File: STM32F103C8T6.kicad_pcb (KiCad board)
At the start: 2 copper layers, 39.4 x 77.5 mm, 55 parts, among them J1 USB_Device, J2 USB_TTL, P1 L-Pin, P2 R-Pin, P3 DEBUG, P4 POWER-R, P5 POWER-L, SW1 NRST, U1 MIC5219-3.3YM5, U2 CH340E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

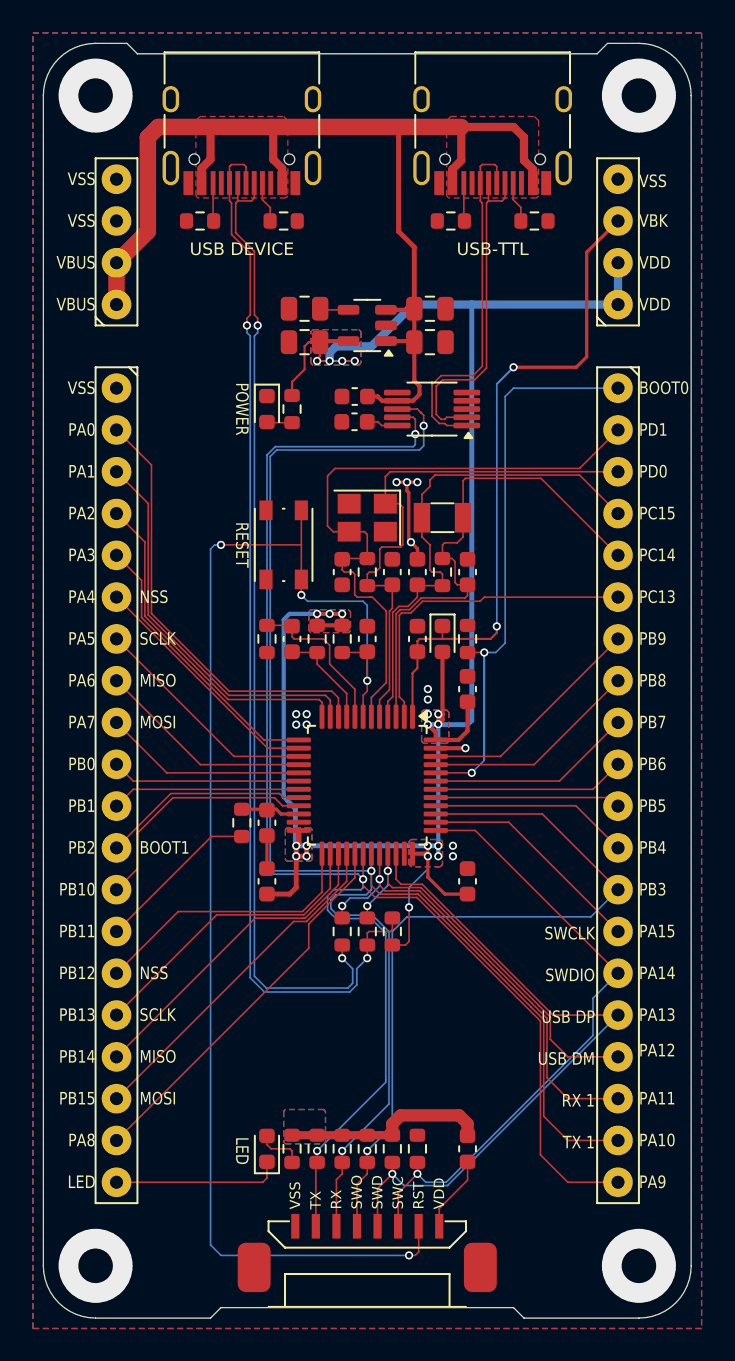
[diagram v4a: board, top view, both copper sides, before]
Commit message: 优化电源走线
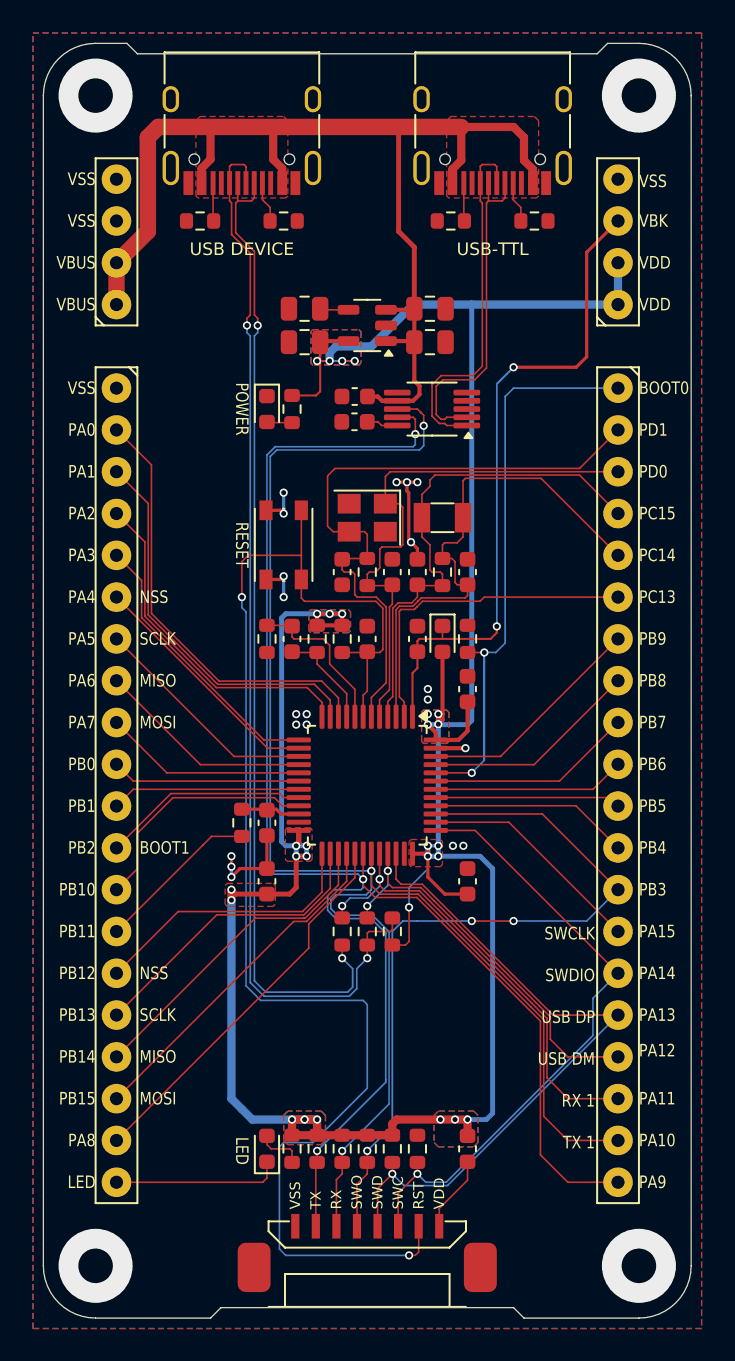
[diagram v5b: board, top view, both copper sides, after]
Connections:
- C15 pad 1: VSS -> VDD
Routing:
- net VDD: track 140.0 -> 191.5 mm, vias 20 -> 28
- net VSS: track 10.0 -> 18.5 mm, vias 13 -> 20
- net /NRST: track 82.1 -> 85.5 mm, vias 4 -> 2
- net /USBF_N: track 59.8 -> 60.4 mm
- net /USBF_P: track 64.9 -> 65.4 mm
- net /PB3/SWO: vias 1 -> 3

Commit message: 更新引脚链接，增加晶振引脚的跳接焊盘
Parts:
- added H1: M2 Hole, Append_Connector:Hole_2×4.5mm, F.Cu at (133.5, 82.5)
- added H2: M2 Hole, Append_Connector:Hole_2×4.5mm, F.Cu at (166.5, 82.5)
- added H3: M2 Hole, Append_Connector:Hole_2×4.5mm, F.Cu at (133.5, 153.7)
- added H4: M2 Hole, Append_Connector:Hole_2×4.5mm, F.Cu at (166.5, 153.7)
- added TP1: PD1, Append_Connector:PAD_Semicircular_1mm, F.Cu at (147.6, 109.1)
- added TP2: PD0, Append_Connector:PAD_Semicircular_1mm, F.Cu at (151.1, 106.2)
- added TP3: PC15, Append_Connector:PAD_Semicircular_1mm, F.Cu at (153.3, 106.8)
- added TP4: PC14, Append_Connector:PAD_Semicircular_1mm, F.Cu at (155.8, 106.8)
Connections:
- P2 pad 2: /PD1/OSC_OUT -> /PD1
- P2 pad 3: /PD0/OSC_IN -> /PD0
- P2 pad 4: /PC15/OSC32_OUT -> /PC15
- P2 pad 5: /PC14/OSC32_IN -> /PC14
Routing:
- net /PD1/OSC_OUT: track 39.5 -> 16.2 mm
- net /PD1: track 0.00 -> 23.1 mm
- net /PD0/OSC_IN: track 33.5 -> 17.6 mm
- net /PC15/OSC32_OUT: track 30.7 -> 15.7 mm
- net /PD0: track 0.00 -> 14.7 mm
- net /PC14/OSC32_IN: track 31.9 -> 18.2 mm
- net /PC15: track 0.00 -> 13.6 mm
- net /PC14: track 0.00 -> 12.0 mm
- net /PB3/SWO: track 46.7 -> 47.2 mm
- net VSS: track 18.5 -> 18.1 mm, vias 20 -> 19
- net (no net): vias 4 -> 0

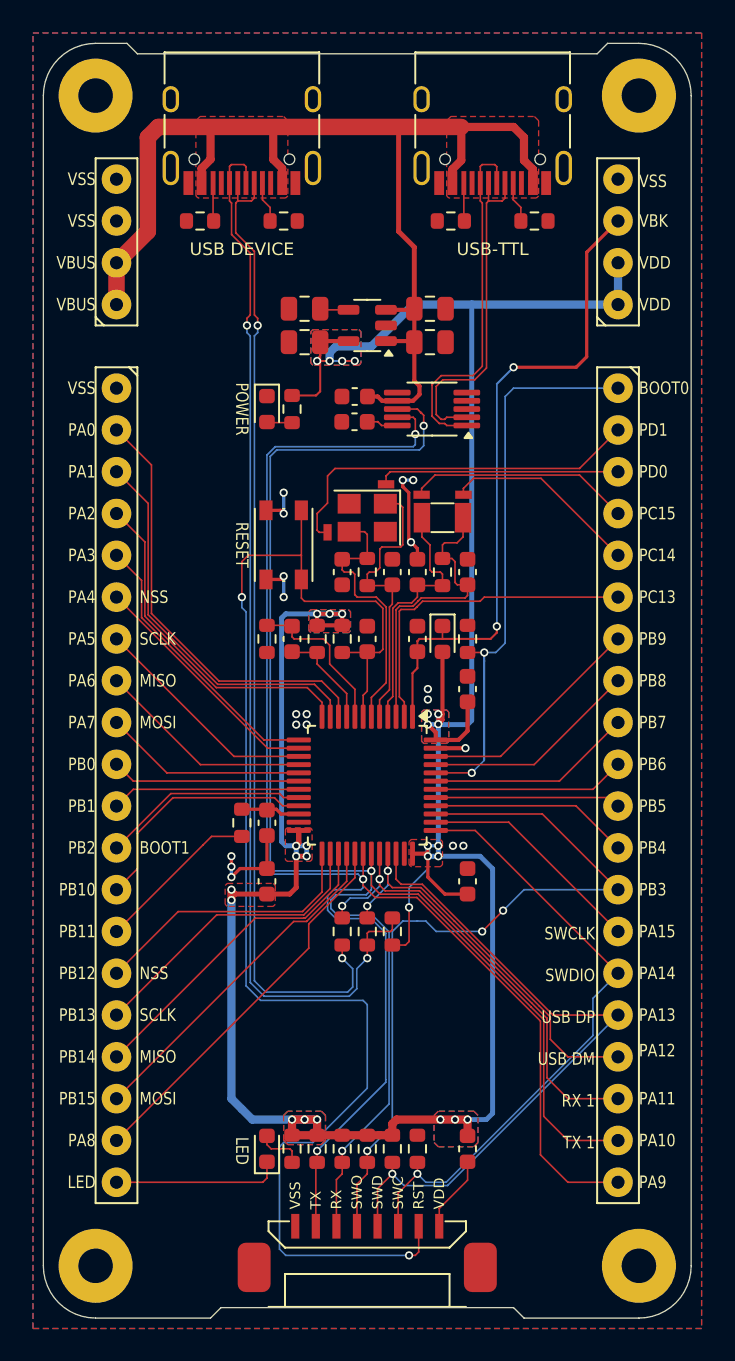
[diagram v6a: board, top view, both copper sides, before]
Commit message: 优化电源走线
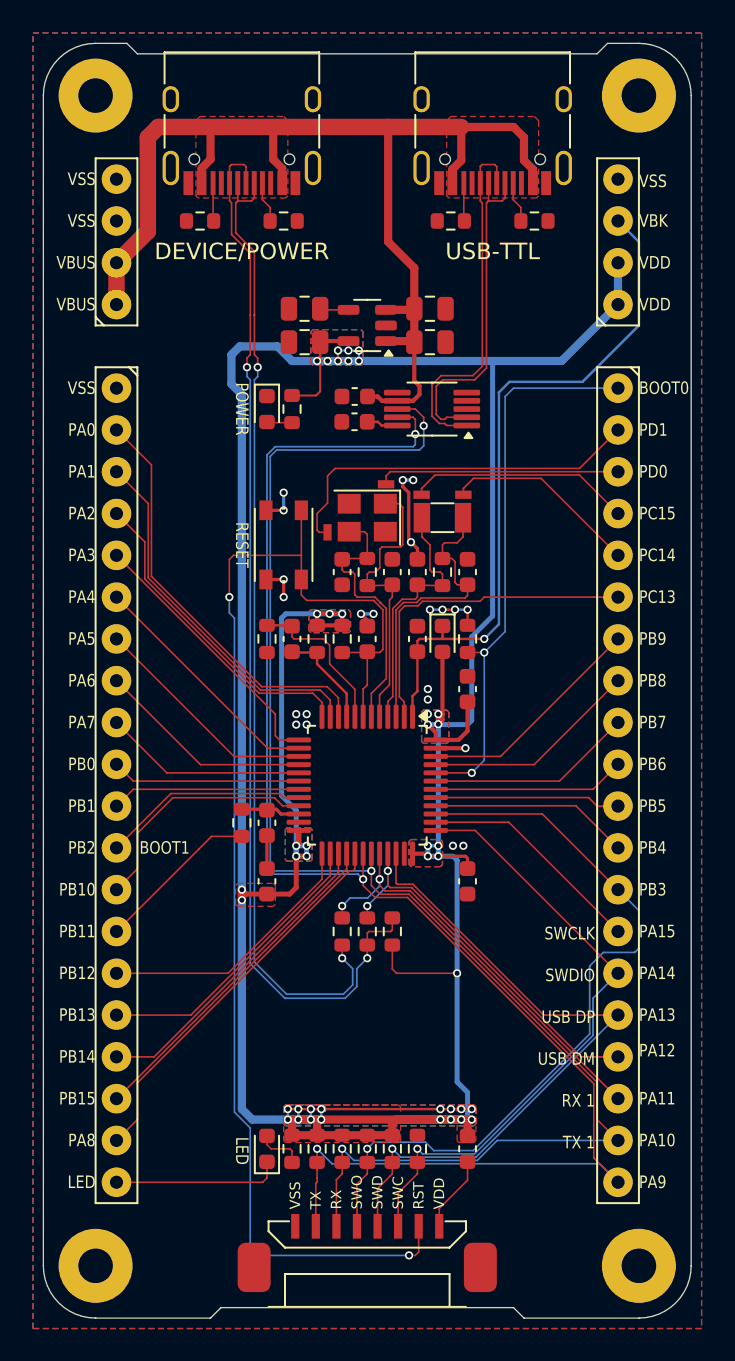
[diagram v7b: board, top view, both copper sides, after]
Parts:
- turned C15 to -90 degrees
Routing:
- net VDD: track 191.5 -> 248.5 mm, vias 28 -> 42
- net VBUS: track 86.6 -> 72.0 mm
- net /PA10/USART_RX: track 99.3 -> 91.5 mm
- net /NRST: track 85.5 -> 78.2 mm
- net /BOOT0: track 41.1 -> 34.0 mm
- net /PA9/USART_TX: track 100.5 -> 94.7 mm
- net /PA11/USBDM: track 27.9 -> 25.7 mm
- net /PA0/WAKEUP: track 26.7 -> 25.3 mm
- net /PA1: track 23.7 -> 22.4 mm
- net /PA2: track 20.8 -> 19.4 mm
- net VBAT: track 40.8 -> 42.1 mm, vias 2 -> 1
- net /PB3/SWO: track 47.2 -> 46.4 mm, vias 3 -> 1
- net /PA12/USBDP: track 24.3 -> 23.6 mm
- net /USBF_P: track 65.4 -> 64.7 mm
- net /PA3: track 17.0 -> 16.5 mm
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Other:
- board text added: "DEVICE/POWER"
- board text removed: "MISO"
- board text removed: "MOSI"
- board text removed: "NSS"
- board text removed: "SCLK"
- board text removed: "USB DEVICE"

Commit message: 修改调试器接口的电源走线
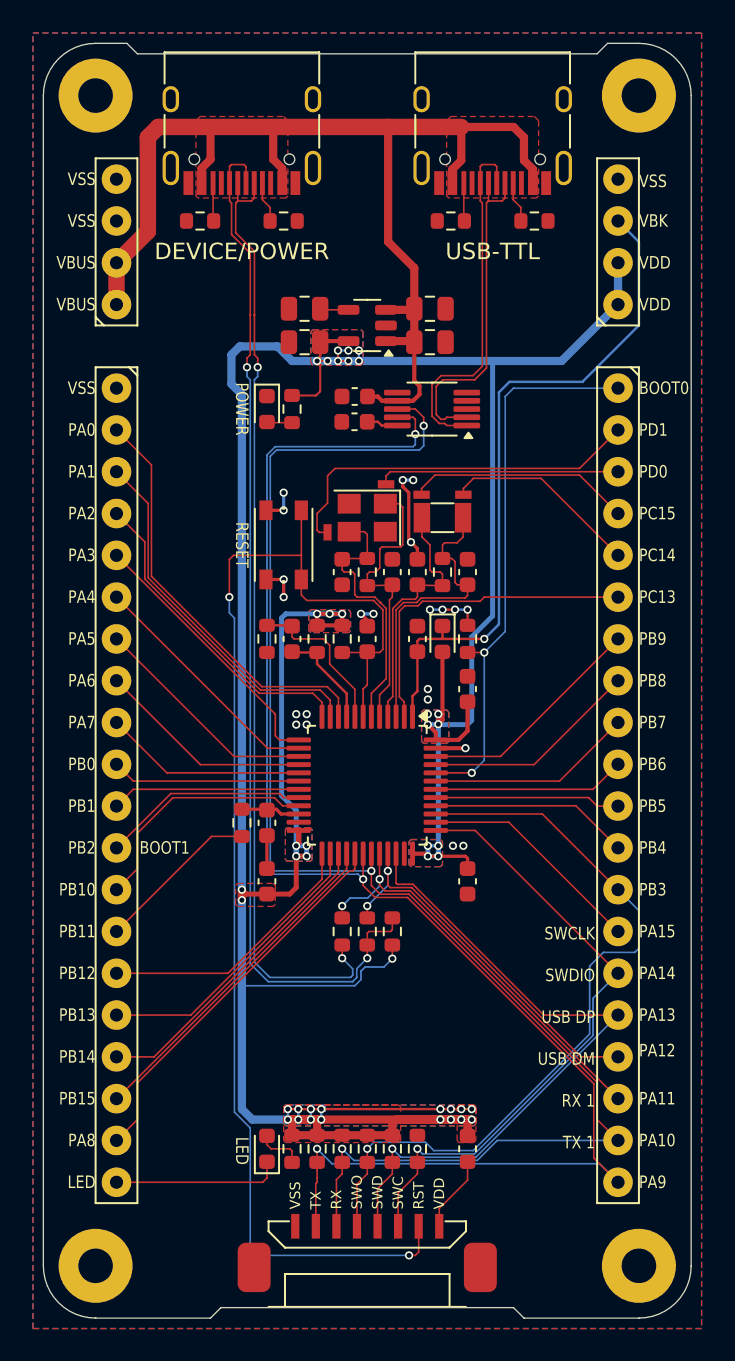
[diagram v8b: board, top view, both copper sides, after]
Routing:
- net VDD: track 248.5 -> 236.1 mm
- net /USBF_N: track 59.8 -> 58.6 mm
- net /USBF_P: track 64.7 -> 63.6 mm
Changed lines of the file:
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@@
-	)
-	(segment
-		(start 151.523998 135.626)
-		(end 151.524 134.165)
-		(width 0.1)
-		(layer "F.Cu")
-		(net 4)
 	)
 	(segment
@@
 	)
 	(segment
+		(start 151.524 134.165)
+		(end 151.524 134.991)
+		(width 0.1)
+		(layer "F.Cu")
+		(net 4)
+	)
+	(segment
 		(start 146.951999 144.77)
 		(end 146.952 145.723)
@@
 	)
 	(segment
-		(start 151.778 135.879999)
-		(end 151.523998 135.626)
-		(width 0.1)
-		(layer "F.Cu")
-		(net 4)
-	)
-	(segment
 		(start 156.095999 119.383)
 		(end 156.083 119.37)
@@
 	)
 	(segment
-		(start 155.461 135.88)
-		(end 151.778 135.879999)
-		(width 0.1)
-		(layer "F.Cu")
-		(net 4)
-	)
-	(segment
 		(start 156.096009 121.148003)
 		(end 156.095999 119.383)
@@
 	)
 	(via
+		(at 151.524 134.991)
+		(size 0.5)
+		(drill 0.3)
+		(layers "F.Cu" "B.Cu")
+		(net 4)
+	)
+	(via
 		(at 148.476 114.036)
 		(size 0.5)
@@
 	)
 	(via
-		(at 155.461 135.88)
-		(size 0.5)
-		(drill 0.3)
-		(layers "F.Cu" "B.Cu")
-		(net 4)
-	)
-	(via
 		(at 147.206 144.135)
 		(size 0.5)
@@
 		(drill 0.3)
 		(layers "F.Cu" "B.Cu")
+		(net 4)
+	)
+	(segment
+		(start 149.619 136.261)
+		(end 149.242 136.638)
+		(width 0.1)
+		(layer "B.Cu")
+		(net 4)
+	)
+	(segment
+		(start 142.383998 136.638)
+		(end 142.379998 136.642)
+		(width 0.1)
+		(layer "B.Cu")
 		(net 4)
 	)
@@
 		(end 157.62 98.669001)
 		(width 0.5)
-		(layer "B.Cu")
-		(net 4)
-	)
-	(segment
-		(start 155.460999 129.022)
-		(end 155.206999 128.768)
-		(width 0.3)
 		(layer "B.Cu")
 		(net 4)
@@
 	)
 	(segment
+		(start 142.379995 144.135002)
+		(end 142.379998 136.642)
+		(width 0.5)
+		(layer "B.Cu")
+		(net 4)
+	)
+	(segment
 		(start 142.379999 100.701)
 		(end 141.744995 100.066002)
@@
 	)
 	(segment
-		(start 156.095999 143.119)
-		(end 155.460995 142.484002)
-		(width 0.3)
+		(start 151.524 134.991)
+		(end 151.016 135.499)
+		(width 0.1)
 		(layer "B.Cu")
 		(net 4)
@@
 		(start 156.350002 120.513)
 		(end 156.350001 115.433)
-		(width 0.3)
-		(layer "B.Cu")
-		(net 4)
-	)
-	(segment
-		(start 155.206999 128.768)
-		(end 153.683 128.768)
 		(width 0.3)
 		(layer "B.Cu")
@@
 	)
 	(segment
+		(start 151.016 135.499)
+		(end 149.873 135.499)
+		(width 0.1)
+		(layer "B.Cu")
+		(net 4)
+	)
+	(segment
 		(start 153.683 128.768)
 		(end 154.318 128.768)
@@
 	)
 	(segment
+		(start 149.619 135.753)
+		(end 149.619 136.261)
+		(width 0.1)
+		(layer "B.Cu")
+		(net 4)
+	)
+	(segment
 		(start 153.683 128.133)
 		(end 154.318 128.133)
@@
 	)
 	(segment
-		(start 142.379995 144.135002)
-		(end 142.38 131.435)
-		(width 0.5)
-		(layer "B.Cu")
-		(net 4)
-	)
-	(segment
 		(start 142.379999 100.701)
 		(end 142.38 131.435)
@@
 	)
 	(segment
+		(start 149.873 135.499)
+		(end 149.619 135.753)
+		(width 0.1)
+		(layer "B.Cu")
+		(net 4)
+	)
+	(segment
 		(start 161.810998 98.668994)
 		(end 157.62 98.669001)
@@
 	)
 	(segment
+		(start 149.242 136.638)
+		(end 142.383998 136.638)
+		(width 0.1)
+		(layer "B.Cu")
+		(net 4)
+	)
+	(segment
 		(start 144.793001 114.29)
 		(end 145.047 114.035998)
@@
 	)
 	(segment
-		(start 155.460995 142.484002)
-		(end 155.460999 129.022)
-		(width 0.3)
-		(layer "B.Cu")
-		(net 4)
-	)
-	(segment
-		(start 156.095999 143.119)
-		(end 156.096 144.77)
-		(width 0.3)
+		(start 142.379998 136.642)
+		(end 142.38 131.435)
+		(width 0.5)
 		(layer "B.Cu")
 		(net 4)
@@
 	)
 	(segment
-		(start 143.341009 99.613003)
-		(end 143.141001 99.813)
-		(width 0.1)
-		(layer "B.Cu")
-		(net 18)
-	)
-	(segment
-		(start 143.341 99.05)
-		(end 143.341009 99.613003)
-		(width 0.1)
-		(layer "B.Cu")
-		(net 18)
-	)
-	(segment
-		(start 143.141001 99.813)
-		(end 143.140985 135.194227)
-		(width 0.1)
-		(layer "B.Cu")
-		(net 18)
-	)
-	(segment
 		(start 148.476 134.9656)
 		(end 149.112999 135.6026)
@@
 	)
 	(segment
-		(start 148.551221 137.152)
-		(end 149.113006 136.590224)
-		(width 0.1)
-		(layer "B.Cu")
-		(net 18)
-	)
-	(segment
-		(start 148.551221 137.152)
-		(end 145.098778 137.151999)
-		(width 0.1)
-		(layer "B.Cu")
-		(net 18)
-	)
-	(segment
-		(start 149.113006 136.590224)
-		(end 149.112999 135.6026)
-		(width 0.1)
-		(layer "B.Cu")
-		(net 18)
-	)
-	(segment
-		(start 145.098778 137.151999)
+		(start 143.140985 135.194227)
+		(end 143.141001 99.813)
+		(width 0.1)
+		(layer "B.Cu")
+		(net 18)
+	)
+	(segment
+		(start 149.113001 135.88)
+		(end 149.113001 136.004999)
+		(width 0.1)
+		(layer "B.Cu")
+		(net 18)
+	)
+	(segment
+		(start 143.141001 99.813)
+		(end 143.341009 99.613003)
+		(width 0.1)
+		(layer "B.Cu")
+		(net 18)
+	)
+	(segment
+		(start 144.080768 136.134)
+		(end 143.992384 136.045616)
+		(width 0.1)
+		(layer "B.Cu")
+		(net 18)
+	)
+	(segment
+		(start 149.112999 135.6026)
+		(end 149.113001 135.88)
+		(width 0.1)
+		(layer "B.Cu")
+		(net 18)
+	)
+	(segment
+		(start 149.113001 136.004999)
+		(end 148.984 136.134)
+		(width 0.1)
+		(layer "B.Cu")
+		(net 18)
+	)
+	(segment
+		(start 148.984 136.134)
+		(end 144.080768 136.134)
+		(width 0.1)
+		(layer "B.Cu")
+		(net 18)
+	)
+	(segment
+		(start 143.992384 136.045616)
 		(end 143.140985 135.194227)
+		(width 0.1)
+		(layer "B.Cu")
+		(net 18)
+	)
+	(segment
+		(start 143.341009 99.613003)
+		(end 143.341 99.05)
 		(width 0.1)
 		(layer "B.Cu")
@@
 	)
 	(segment
-		(start 144.995222 137.401999)
-		(end 148.654777 137.402)
+		(start 143.981208 136.388)
+		(end 149.109002 136.388)
+		(width 0.1)
+		(layer "B.Cu")
+		(net 19)
+	)
+	(segment
+		(start 142.890999 99.812)
+		(end 142.890987 135.297783)
+		(width 0.1)
+		(layer "B.Cu")
+		(net 19)
+	)
+	(segment
+		(start 149.109002 136.388)
+		(end 149.363002 136.134)
+		(width 0.1)
+		(layer "B.Cu")
+		(net 19)
+	)
+	(segment
+		(start 142.890987 135.297783)
+		(end 143.434604 135.841396)
+		(width 0.1)
+		(layer "B.Cu")
+		(net 19)
+	)
+	(segment
+		(start 149.363002 136.134)
+		(end 149.363001 135.6026)
 		(width 0.1)
 		(layer "B.Cu")
@@
 	)
 	(segment
+		(start 142.690991 99.612003)
+		(end 142.890999 99.812)
+		(width 0.1)
+		(layer "B.Cu")
+		(net 19)
+	)
+	(segment
+		(start 143.434604 135.841396)
+		(end 143.981208 136.388)
+		(width 0.1)
+		(layer "B.Cu")
+		(net 19)
+	)
+	(segment
 		(start 149.363001 135.6026)
 		(end 150 134.9656)
 		(width 0.1)
 		(layer "B.Cu")
-		(net 19)
-	)
-	(segment
-		(start 142.890987 135.297783)
-		(end 144.995222 137.401999)
-		(width 0.1)
-		(layer "B.Cu")
-		(net 19)
-	)
-	(segment
-		(start 149.363001 135.6026)
-		(end 149.363004 136.693779)
-		(width 0.1)
-		(layer "B.Cu")
-		(net 19)
-	)
-	(segment
-		(start 142.890987 135.297783)
-		(end 142.890999 99.812)
-		(width 0.1)
-		(layer "B.Cu")
-		(net 19)
-	)
-	(segment
-		(start 149.363004 136.693779)
-		(end 148.654777 137.402)
-		(width 0.1)
-		(layer "B.Cu")
-		(net 19)
-	)
-	(segment
-		(start 142.890999 99.812)
-		(end 142.690991 99.612003)
-		(width 0.1)
-		(layer "B.Cu")
